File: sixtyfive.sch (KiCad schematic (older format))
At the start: 204 parts, among them J1 Conn_01x12, J2 Conn_ARM_JTAG_SWD_10, Q1 BSS138, SW1 SW_Push, U1 USBLC6-2SC6, U2 STM32F072C8Tx, U3 MCP1700-3302E_SOT23

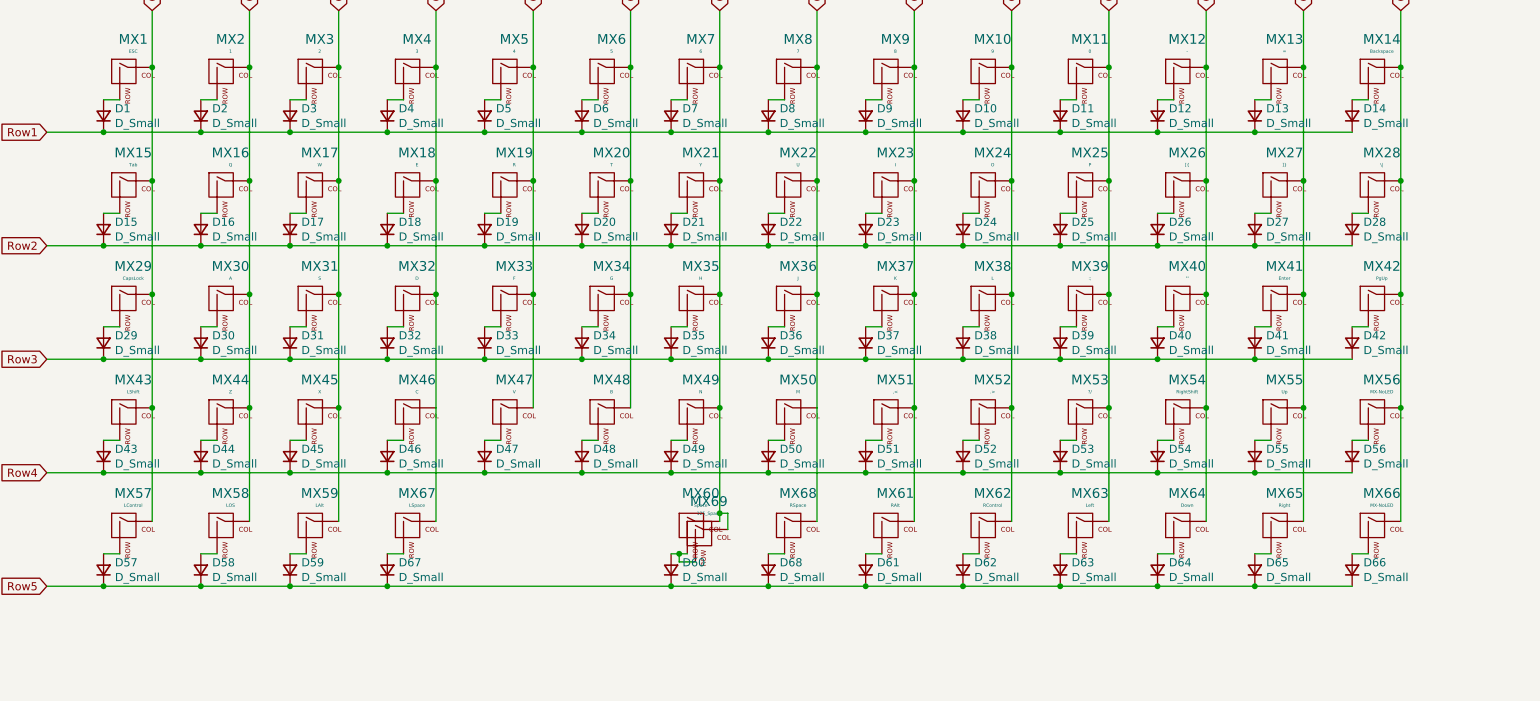
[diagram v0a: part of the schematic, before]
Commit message: Switched some components to "basic" parts, hopefully we good
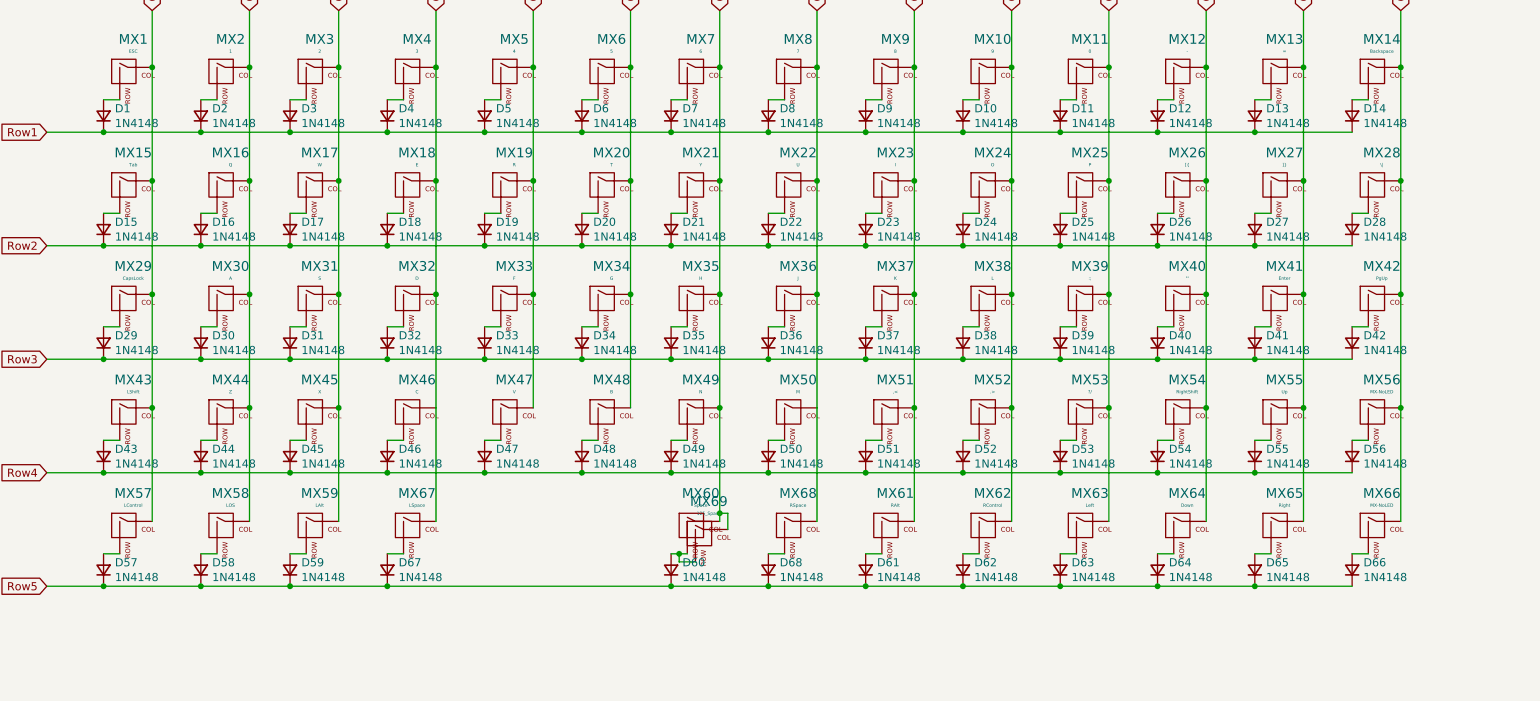
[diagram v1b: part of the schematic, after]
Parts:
- CB1, CB5, CB7, CB8: JLCCode (none) -> C1525
- CB2: JLCCode (none) -> C52923
- CB3: JLCCode (none) -> C15195
- CB4, CB6: JLCCode (none) -> C23733
- CR1: footprint Capacitor_SMD:C_0805_2012Metric_Pad1.15x1.40mm_HandSolder -> Capacitor_SMD:C_0805_2012Metric; JLCCode (none) -> C15850
- CR2: footprint Capacitor_SMD:C_0805_2012Metric_Pad1.15x1.40mm_HandSolder -> Capacitor_SMD:C_0805_2012Metric; JLCCode (none) -> C1744
- CRGB1, CRGB10, CRGB2, CRGB3, CRGB4, CRGB5, CRGB6, CRGB7, CRGB8, CRGB9: JCLPCB (none) -> C49678
- CSH1, CSH2: JLCCode (none) -> C1744
- CSI1, CSO1: footprint Capacitor_SMD:C_0805_2012Metric_Pad1.15x1.40mm_HandSolder -> Capacitor_SMD:C_0805_2012Metric; JLCCode (none) -> C28323
- D1, D10, D11, D12, D13, D14, D15, D16, D17, D18, D19, D2, D20, D21, D22, D23, D24, D25, D26, D27, D28, D29, D3, D30, D31, D32, D33, D34, D35, D36, D37, D38, D39, D4, D40, D41, D42, D43, D44, D45, D46, D47, D48, D49, D5, D50, D51, D52, D53, D54, D55, D56, D57, D58, D59, D6, D60, D61, D62, D63, D64, D65, D66, D67, D68, D7, D8, D9: value D_Small -> 1N4148; JLCCode (none) -> C81598
- DF1: JLCCode (none) -> C123799
- DR1: JLCCode (none) -> C81598
- DS1: JLCCode (none) -> C115330
- F1: JLCCode (none) -> C84140
- MX60: footprint MX_Only:MXOnly-6.25U-Hotswap -> MX_Only:MXOnly-6.25U-Hotswap-ReversedStabilizers
- MX67: footprint MX_Only:MXOnly-2.75U-Hotswap-ReversedStabilizers -> MX_Only:MXOnly-2.75U-Hotswap
- MX68: footprint MX_Only:MXOnly-2.25U-Hotswap-ReversedStabilizers -> MX_Only:MXOnly-2.25U-Hotswap
- Q1: JLCCode (none) -> C193019
- QRST1: JLCCode (none) -> C111724
- RCC1, RCC2: footprint Resistor_SMD:R_1206_3216Metric -> Resistor_SMD:R_0805_2012Metric; JLCCode (none) -> C27834
- RGND1: JLCCode (none) -> C127703
- RR1, RSI1, RSO1: JLCCode (none) -> C17900
- RRGB1, RRGB10, RRGB2, RRGB3, RRGB4, RRGB5, RRGB6, RRGB7, RRGB8, RRGB9: footprint Resistor_SMD:R_1206_3216Metric -> Resistor_SMD:R_0805_2012Metric; JLCCode (none) -> C17724
- RS1, RS2: JLCCode (none) -> C17902
- RSH1, RSH2: footprint Resistor_SMD:R_1206_3216Metric -> Resistor_SMD:R_0805_2012Metric; JLCCode (none) -> C17514
- SW1: JLCCode (none) -> C318884
- U1: JLCPCB (none) -> C7519
- U2: JLCCode (none) -> C80488
- U3: JLCCode (none) -> C39051

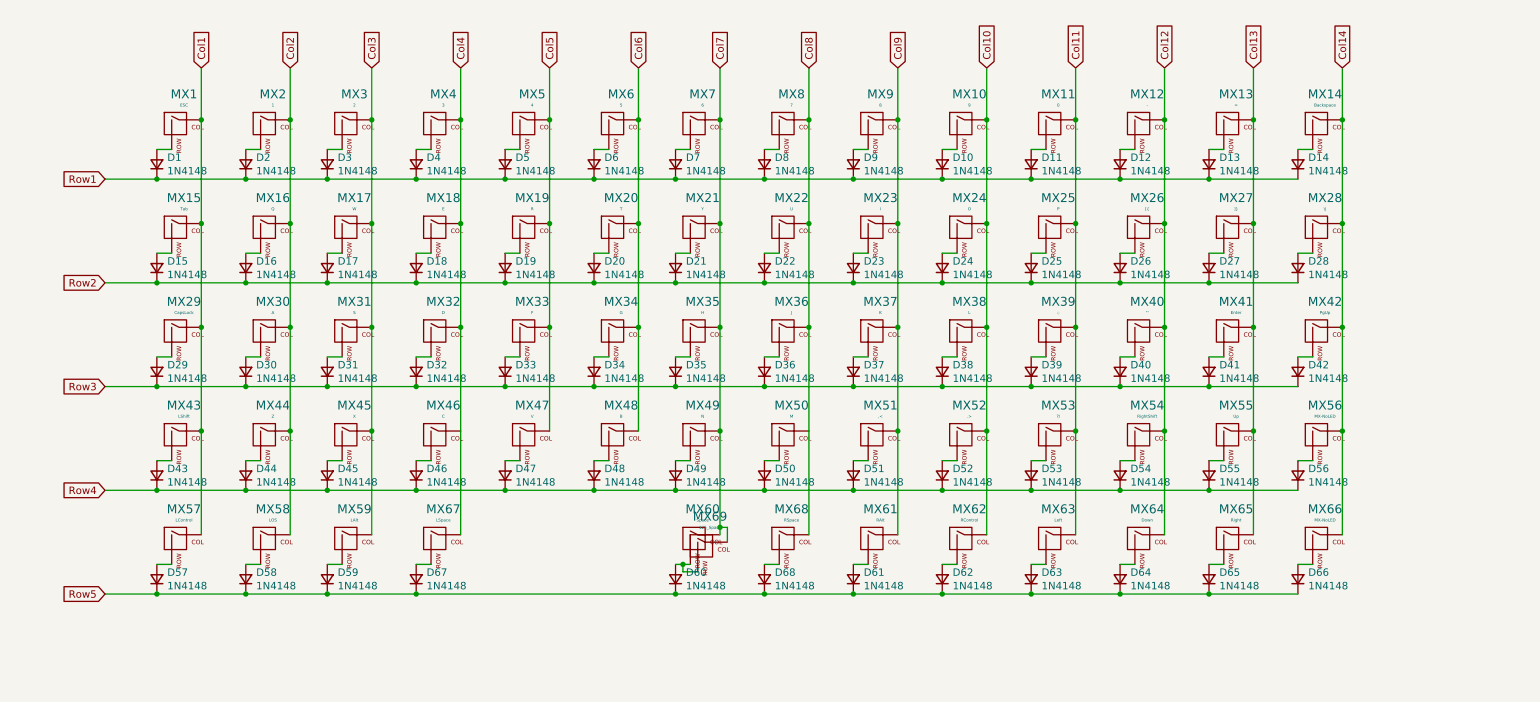
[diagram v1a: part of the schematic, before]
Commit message: Redoing literally all the routing, switched diodes to common anode
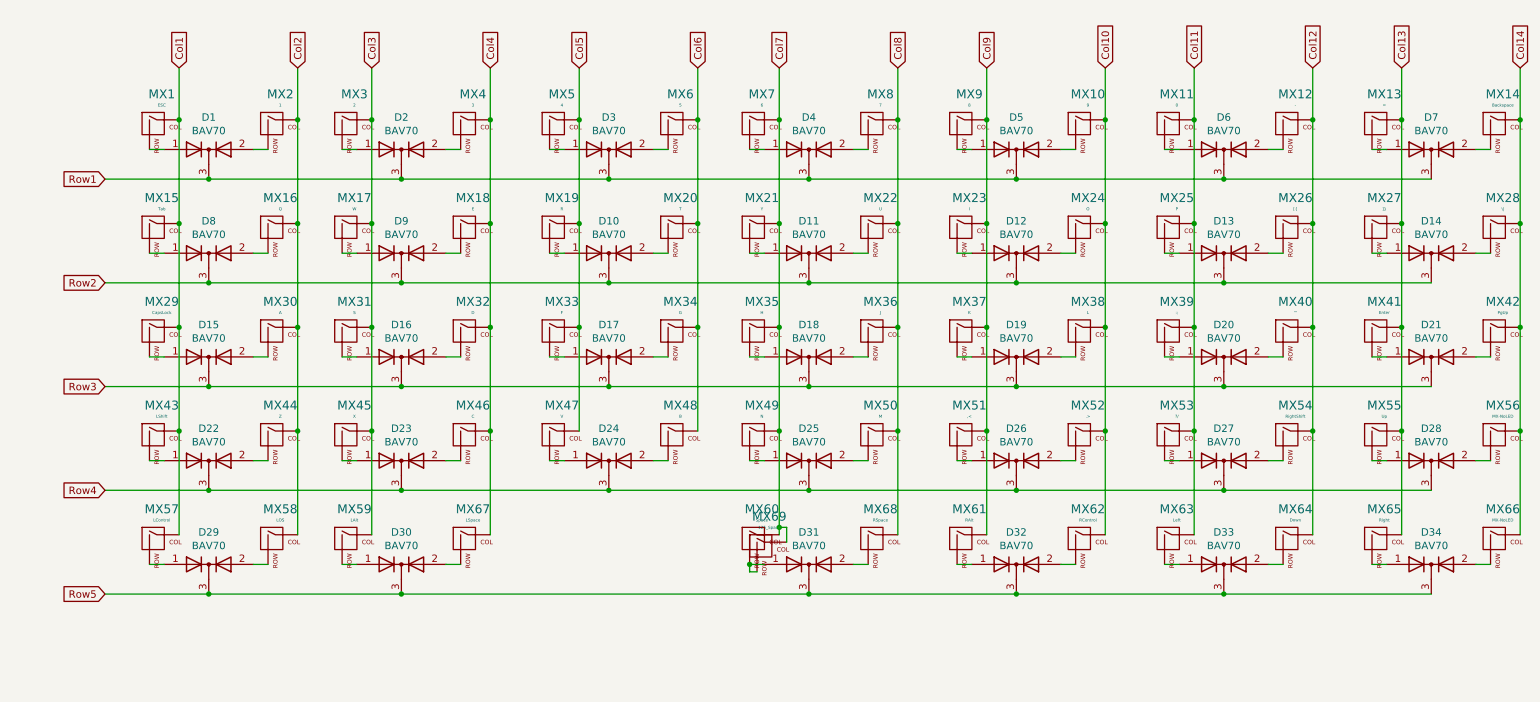
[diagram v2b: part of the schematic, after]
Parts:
- removed D1, D10, D11, D12, D13, D14, D15, D16, D17, D18, D19, D2, D20, D21, D22, D23, D24, D25, D26, D27, D28, D29, D3, D30, D31, D32, D33, D34, D35, D36, D37, D38, D39, D4, D40, D41, D42, D43, D44, D45, D46, D47, D48, D49, D5, D50, D51, D52, D53, D54, D55, D56, D57, D58, D59, D6, D60, D61, D62, D63, D64, D65, D66, D67, D68, D7, D8, D9: 1N4148, Diode_SMD:D_SOD-123, symbol Device:D_Small
- added D1, D10, D11, D12, D13, D14, D15, D16, D17, D18, D19, D2, D20, D21, D22, D23, D24, D25, D26, D27, D28, D29, D3, D30, D31, D32, D33, D34, D4, D5, D6, D7, D8, D9: BAV70, Package_TO_SOT_SMD:SOT-23, symbol Diode:BAV70
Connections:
- wire segments 491 -> 456
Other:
- moved on the sheet: MX1, MX10, MX11, MX12, MX13, MX14, MX15, MX16, MX18, MX19, MX2, MX20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

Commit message: Rerouted everything, feels cleaner now?
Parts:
- removed DS1: RB060M-60TR, Diode_SMD:D_SOD-123, symbol Device:D_Schottky
- removed RSO1: 100k, Resistor_SMD:R_1206_3216Metric, symbol Device:R_Small
- added DS1: SM4007, Diode_SMD:D_SOD-123F, symbol Diode:SM4007
- RSI1: value 100k -> 1M; footprint Resistor_SMD:R_1206_3216Metric -> Resistor_SMD:R_0805_2012Metric; JLCCode C17900 -> C17514
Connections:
- wire segments 456 -> 454
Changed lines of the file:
@@
 Connection ~ 24450 20850
 $Comp
-L Device:D_Schottky DS1
-U 1 1 5F10829E
-P 25050 20300
-F 0 "DS1" H 25050 20517 50  0000 C CNN
-F 1 "RB060M-60TR" H 25050 20426 50  0000 C CNN
-F 2 "Diode_SMD:D_SOD-123" H 25050 20300 50  0001 C CNN
-F 3 "~" H 25050 20300 50  0001 C CNN
-F 4 "C115330" H 25050 20300 50  0001 C CNN "JLCCode"
-	1    25050 20300
-	1    0    0    -1
-$EndComp
-$Comp
 L Device:C_Small CSI1
 U 1 1 5F108D1D
@@
 	25050 21650 25350 21650
 $Comp
-L Device:R_Small RSO1
-U 1 1 5F10AD87
-P 25550 20950
-F 0 "RSO1" H 25609 20996 50  0000 L CNN
-F 1 "100k" H 25609 20905 50  0000 L CNN
-F 2 "Resistor_SMD:R_1206_3216Metric" H 25550 20950 50  0001 C CNN
-F 3 "~" H 25550 20950 50  0001 C CNN
-F 4 "C17900" H 25550 20950 50  0001 C CNN "JLCCode"
-	1    25550 20950
-	1    0    0    -1
-$EndComp
-$Comp
 L Device:R_Small RSI1
 U 1 1 5F10576E
 P 24450 21000
 F 0 "RSI1" H 24509 21046 50  0000 L CNN
-F 1 "100k" H 24509 20955 50  0000 L CNN
-F 2 "Resistor_SMD:R_1206_3216Metric" H 24450 21000 50  0001 C CNN
+F 1 "1M" H 24509 20955 50  0000 L CNN
+F 2 "Resistor_SMD:R_0805_2012Metric" H 24450 21000 50  0001 C CNN
 F 3 "~" H 24450 21000 50  0001 C CNN
-F 4 "C17900" H 24450 21000 50  0001 C CNN "JLCCode"
+F 4 "C17514" H 24450 21000 50  0001 C CNN "JLCCode"
 	1    24450 21000
 	1    0    0    -1
@@
 	1    0    0    -1
 $EndComp
-$Comp
-L power:GND #PWR0103
-U 1 1 5F10D25F
-P 25550 21250
-F 0 "#PWR0103" H 25550 21000 50  0001 C CNN
-F 1 "GND" H 25555 21077 50  0000 C CNN
-F 2 "" H 25550 21250 50  0001 C CNN
-F 3 "" H 25550 21250 50  0001 C CNN
-	1    25550 21250
-	1    0    0    -1
-$EndComp
-Wire Wire Line
-	25550 21050 25550 21250
 Wire Wire Line
 	24450 21100 24450 21250
@@
 Text GLabel 25800 20850 2    50   Output ~ 0
 3.3V
-Wire Wire Line
-	25800 20850 25550 20850
 Text GLabel 23500 20850 0    50   Input ~ 0
 VBUS
@@
 Wire Wire Line
 	25050 21150 25050 21650
-Wire Wire Line
-	25350 20850 25550 20850
-Connection ~ 25550 20850
 Text GLabel 28700 15800 0    50   Input ~ 0
 3.3V
@@
 Col6
 Text GLabel 28150 17400 0    50   Input ~ 0
-Row5
+Row4
 Text GLabel 28150 17300 0    50   Input ~ 0
 Col9
@@
 Extra5
 Text GLabel 28150 17500 0    50   Input ~ 0
-Row4
+Row5
 Text GLabel 28150 17800 0    50   Input ~ 0
 Extra3
@@
 Wire Wire Line
 	24500 11600 24600 11600
+$Comp
+L Diode:SM4007 DS1
+U 1 1 5EEB7751
+P 25050 20300
+F 0 "DS1" H 25050 20517 50  0000 C CNN
+F 1 "SM4007" H 25050 20426 50  0000 C CNN
+F 2 "Diode_SMD:D_SOD-123F" H 25050 20125 50  0001 C CNN
+F 3 "http://cdn-reichelt.de/documents/datenblatt/A400/SMD1N400%23DIO.pdf" H 25050 20300 50  0001 C CNN
+F 4 "C64898" H 25050 20300 50  0001 C CNN "JLCCode"
+	1    25050 20300
+	1    0    0    -1
+$EndComp
+Wire Wire Line
+	25350 20850 25800 20850
 $EndSCHEMATC
